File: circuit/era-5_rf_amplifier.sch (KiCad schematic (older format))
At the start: 9 parts, among them J1 CONN_01X04, J2 CONN_01X04, U1 ERA-5+

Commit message: rearranged schematics
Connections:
- net RFin: now reaches C1.2, J1.2 (P2), J1.3 (P3)
- net RFout: now reaches C2.1, J2.3 (P3)
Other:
- moved on the sheet: C1, C2, C3, L1, R1, R2
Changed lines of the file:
@@
 L C C1
 U 1 1 5931B134
-P 2550 2800
-F 0 "C1" H 2575 2900 50  0000 L CNN
-F 1 "0.1µF" H 2575 2700 50  0000 L CNN
-F 2 "" H 2588 2650 50  0001 C CNN
-F 3 "" H 2550 2800 50  0001 C CNN
-	1    2550 2800
+P 2850 2800
+F 0 "C1" H 2875 2900 50  0000 L CNN
+F 1 "0.1µF" H 2875 2700 50  0000 L CNN
+F 2 "" H 2888 2650 50  0001 C CNN
+F 3 "" H 2850 2800 50  0001 C CNN
+	1    2850 2800
 	0    1    1    0
 $EndComp
@@
 L C C2
 U 1 1 5931B1E4
-P 5150 2800
-F 0 "C2" H 5175 2900 50  0000 L CNN
-F 1 "0.1µF" H 5175 2700 50  0000 L CNN
-F 2 "" H 5188 2650 50  0001 C CNN
-F 3 "" H 5150 2800 50  0001 C CNN
-	1    5150 2800
+P 4800 2800
+F 0 "C2" H 4825 2900 50  0000 L CNN
+F 1 "0.1µF" H 4825 2700 50  0000 L CNN
+F 2 "" H 4838 2650 50  0001 C CNN
+F 3 "" H 4800 2800 50  0001 C CNN
+	1    4800 2800
 	0    1    1    0
 $EndComp
@@
 L L L1
 U 1 1 5931B2E5
-P 4850 2500
-F 0 "L1" V 4800 2500 50  0000 C CNN
-F 1 "1.59µH" V 4925 2500 50  0000 C CNN
-F 2 "" H 4850 2500 50  0001 C CNN
-F 3 "" H 4850 2500 50  0001 C CNN
-	1    4850 2500
+P 4500 2500
+F 0 "L1" V 4450 2500 50  0000 C CNN
+F 1 "1.59µH" V 4575 2500 50  0000 C CNN
+F 2 "" H 4500 2500 50  0001 C CNN
+F 3 "" H 4500 2500 50  0001 C CNN
+	1    4500 2500
 	1    0    0    -1
 $EndComp
@@
 L R R2
 U 1 1 5931B3DD
-P 5200 2050
-F 0 "R2" V 5280 2050 50  0000 C CNN
-F 1 "100R" V 5200 2050 50  0000 C CNN
-F 2 "" V 5130 2050 50  0001 C CNN
-F 3 "" H 5200 2050 50  0001 C CNN
-	1    5200 2050
+P 5200 1700
+F 0 "R2" V 5280 1700 50  0000 C CNN
+F 1 "100R" V 5200 1700 50  0000 C CNN
+F 2 "" V 5130 1700 50  0001 C CNN
+F 3 "" H 5200 1700 50  0001 C CNN
+	1    5200 1700
 	0    1    1    0
 $EndComp
@@
 L R R1
 U 1 1 5931B444
-P 5200 1850
-F 0 "R1" V 5280 1850 50  0000 C CNN
-F 1 "100R" V 5200 1850 50  0000 C CNN
-F 2 "" V 5130 1850 50  0001 C CNN
-F 3 "" H 5200 1850 50  0001 C CNN
-	1    5200 1850
+P 5200 1500
+F 0 "R1" V 5280 1500 50  0000 C CNN
+F 1 "100R" V 5200 1500 50  0000 C CNN
+F 2 "" V 5130 1500 50  0001 C CNN
+F 3 "" H 5200 1500 50  0001 C CNN
+	1    5200 1500
 	0    1    1    0
 $EndComp
@@
 L C C3
 U 1 1 5931B556
+P 5800 1850
+F 0 "C3" H 5825 1950 50  0000 L CNN
+F 1 "0.1µF" H 5825 1750 50  0000 L CNN
+F 2 "" H 5838 1700 50  0001 C CNN
+F 3 "" H 5800 1850 50  0001 C CNN
+	1    5800 1850
+	1    0    0    -1
+$EndComp
+$Comp
+L GND #PWR01
+U 1 1 5931B719
 P 5800 2200
-F 0 "C3" H 5825 2300 50  0000 L CNN
-F 1 "0.1µF" H 5825 2100 50  0000 L CNN
-F 2 "" H 5838 2050 50  0001 C CNN
+F 0 "#PWR01" H 5800 1950 50  0001 C CNN
+F 1 "GND" H 5800 2050 50  0000 C CNN
+F 2 "" H 5800 2200 50  0001 C CNN
 F 3 "" H 5800 2200 50  0001 C CNN
 	1    5800 2200
@@
 $EndComp
 $Comp
-L GND #PWR01
-U 1 1 5931B719
-P 5800 2550
-F 0 "#PWR01" H 5800 2300 50  0001 C CNN
-F 1 "GND" H 5800 2400 50  0000 C CNN
-F 2 "" H 5800 2550 50  0001 C CNN
-F 3 "" H 5800 2550 50  0001 C CNN
-	1    5800 2550
-	1    0    0    -1
-$EndComp
-$Comp
 L VCC #PWR02
 U 1 1 5931B73F
-P 5800 1550
-F 0 "#PWR02" H 5800 1400 50  0001 C CNN
-F 1 "VCC" H 5800 1700 50  0000 C CNN
-F 2 "" H 5800 1550 50  0001 C CNN
-F 3 "" H 5800 1550 50  0001 C CNN
-	1    5800 1550
-	1    0    0    -1
-$EndComp
-Wire Wire Line
-	5800 2350 5800 2550
-Wire Wire Line
-	5800 1550 5800 2050
-Wire Wire Line
-	5350 1850 5350 2050
-Wire Wire Line
-	5350 1950 5800 1950
-Connection ~ 5800 1950
-Connection ~ 5350 1950
-Wire Wire Line
-	5050 1850 5050 2050
-Wire Wire Line
-	4850 2350 4850 1950
-Wire Wire Line
-	4850 1950 5050 1950
-Connection ~ 5050 1950
-Wire Wire Line
-	4850 2650 4850 2800
-Wire Wire Line
-	4300 2800 5000 2800
+P 5800 1200
+F 0 "#PWR02" H 5800 1050 50  0001 C CNN
+F 1 "VCC" H 5800 1350 50  0000 C CNN
+F 2 "" H 5800 1200 50  0001 C CNN
+F 3 "" H 5800 1200 50  0001 C CNN
+	1    5800 1200
+	1    0    0    -1
+$EndComp
+Wire Wire Line
+	5800 2000 5800 2200
+Wire Wire Line
+	5800 1200 5800 1700
+Wire Wire Line
+	5350 1500 5350 1700
+Wire Wire Line
+	5350 1600 5800 1600
+Connection ~ 5800 1600
+Connection ~ 5350 1600
+Wire Wire Line
+	5050 1500 5050 1700
+Wire Wire Line
+	4500 1600 5050 1600
+Connection ~ 5050 1600
 $Comp
 L CONN_01X04 J1
@@
 	2050 2750 2050 2850
 Wire Wire Line
-	2050 2800 2400 2800
+	2050 2800 2700 2800
 Connection ~ 2050 2800
 $Comp
@@
 	2150 2950 2150 3150
 Wire Wire Line
-	5300 2800 5600 2800
+	4950 2800 5600 2800
 Wire Wire Line
 	5600 2800 5600 3350
@@
 Wire Wire Line
 	5200 3250 5200 3500
-Connection ~ 4850 2800
-Wire Wire Line
-	2700 2800 3100 2800
 $Comp
 L ERA-5+ U1
@@
 Wire Wire Line
 	1100 750  1100 900
+Text Label 5350 2800 0    60   ~ 0
+RFout
+Wire Wire Line
+	3000 2800 3100 2800
+Text Label 2450 2800 0    60   ~ 0
+RFin
+Wire Wire Line
+	4650 2800 4300 2800
+Wire Wire Line
+	4500 2650 4500 2800
+Connection ~ 4500 2800
+Wire Wire Line
+	4500 1600 4500 2350
 $EndSCHEMATC

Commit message: added some footprints
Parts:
- C1, C2, C3: footprint (none) -> Capacitors_SMD:C_1210_HandSoldering
- R1, R2: footprint (none) -> Resistors_SMD:R_1210_HandSoldering
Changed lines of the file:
@@
 LIBS:mc-amplifiers
 LIBS:rfcom
+LIBS:mc-chokes
 LIBS:era-5_rf_amplifier-cache
 EELAYER 25 0
@@
 F 0 "C1" H 2875 2900 50  0000 L CNN
 F 1 "0.1µF" H 2875 2700 50  0000 L CNN
-F 2 "" H 2888 2650 50  0001 C CNN
+F 2 "Capacitors_SMD:C_1210_HandSoldering" H 2888 2650 50  0001 C CNN
 F 3 "" H 2850 2800 50  0001 C CNN
 	1    2850 2800
@@
 F 0 "C2" H 4825 2900 50  0000 L CNN
 F 1 "0.1µF" H 4825 2700 50  0000 L CNN
-F 2 "" H 4838 2650 50  0001 C CNN
+F 2 "Capacitors_SMD:C_1210_HandSoldering" H 4838 2650 50  0001 C CNN
 F 3 "" H 4800 2800 50  0001 C CNN
 	1    4800 2800
@@
 F 0 "R2" V 5280 1700 50  0000 C CNN
 F 1 "100R" V 5200 1700 50  0000 C CNN
-F 2 "" V 5130 1700 50  0001 C CNN
+F 2 "Resistors_SMD:R_1210_HandSoldering" V 5130 1700 50  0001 C CNN
 F 3 "" H 5200 1700 50  0001 C CNN
 	1    5200 1700
@@
 F 0 "R1" V 5280 1500 50  0000 C CNN
 F 1 "100R" V 5200 1500 50  0000 C CNN
-F 2 "" V 5130 1500 50  0001 C CNN
+F 2 "Resistors_SMD:R_1210_HandSoldering" V 5130 1500 50  0001 C CNN
 F 3 "" H 5200 1500 50  0001 C CNN
 	1    5200 1500
@@
 F 0 "C3" H 5825 1950 50  0000 L CNN
 F 1 "0.1µF" H 5825 1750 50  0000 L CNN
-F 2 "" H 5838 1700 50  0001 C CNN
+F 2 "Capacitors_SMD:C_1210_HandSoldering" H 5838 1700 50  0001 C CNN
 F 3 "" H 5800 1850 50  0001 C CNN
 	1    5800 1850

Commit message: footprint for inductor
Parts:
- L1: footprint (none) -> Inductors_SMD:L_1812_HandSoldering
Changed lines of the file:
@@
 F 0 "L1" V 4450 2500 50  0000 C CNN
 F 1 "1.59µH" V 4575 2500 50  0000 C CNN
-F 2 "" H 4500 2500 50  0001 C CNN
+F 2 "Inductors_SMD:L_1812_HandSoldering" H 4500 2500 50  0001 C CNN
 F 3 "" H 4500 2500 50  0001 C CNN
 	1    4500 2500

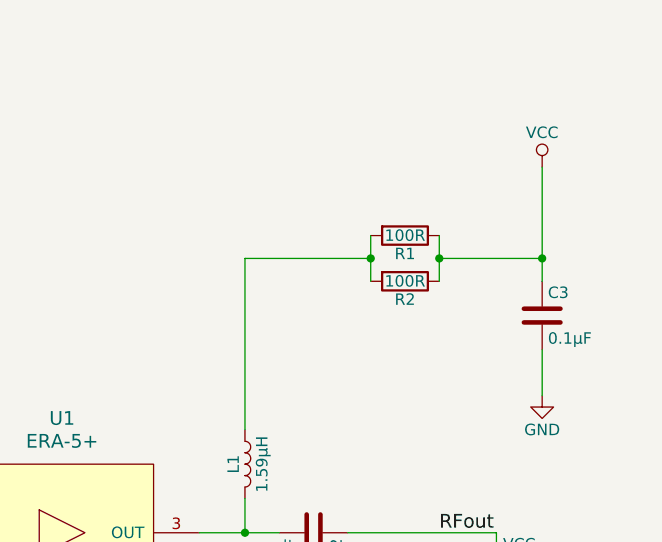
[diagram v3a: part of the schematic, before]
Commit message: Modified board schematic and layout
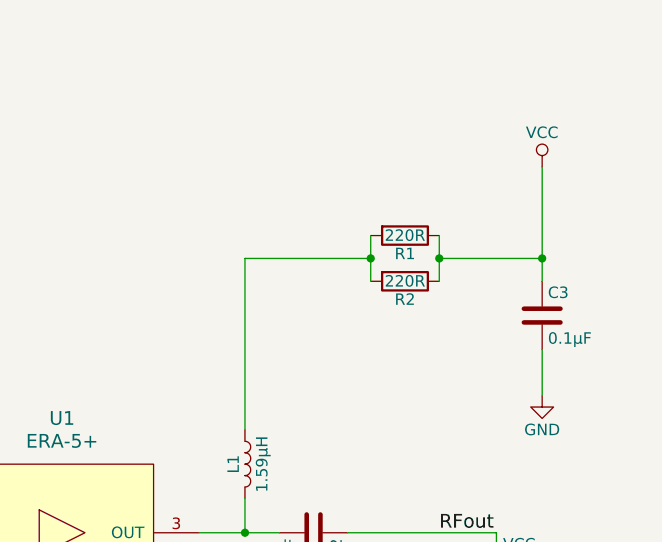
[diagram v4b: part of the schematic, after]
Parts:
- C1, C2, C3: footprint Capacitors_SMD:C_1210_HandSoldering -> Capacitors_SMD:C_1206_HandSoldering
- J1, J2: footprint Pin_Headers:Pin_Header_Straight_1x04_Pitch2.00mm -> Pin_Headers:Pin_Header_Straight_1x04_Pitch2.54mm
- R1, R2: value 100R -> 220R; footprint Resistors_SMD:R_1210_HandSoldering -> Resistors_SMD:R_1206_HandSoldering
- U1: footprint MiniCircuits:WW107 -> MiniCircuits:VV105
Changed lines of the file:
@@
 Sheet 1 1
 Title "ERA-5 amplifier"
-Date ""
+Date "2017-06-07"
 Rev ""
 Comp ""
@@
 F 0 "C1" H 2875 2900 50  0000 L CNN
 F 1 "0.1µF" H 2875 2700 50  0000 L CNN
-F 2 "Capacitors_SMD:C_1210_HandSoldering" H 2888 2650 50  0001 C CNN
+F 2 "Capacitors_SMD:C_1206_HandSoldering" H 2888 2650 50  0001 C CNN
 F 3 "" H 2850 2800 50  0001 C CNN
 	1    2850 2800
@@
 F 0 "C2" H 4825 2900 50  0000 L CNN
 F 1 "0.1µF" H 4825 2700 50  0000 L CNN
-F 2 "Capacitors_SMD:C_1210_HandSoldering" H 4838 2650 50  0001 C CNN
+F 2 "Capacitors_SMD:C_1206_HandSoldering" H 4838 2650 50  0001 C CNN
 F 3 "" H 4800 2800 50  0001 C CNN
 	1    4800 2800
@@
 P 5200 1700
 F 0 "R2" V 5280 1700 50  0000 C CNN
-F 1 "100R" V 5200 1700 50  0000 C CNN
-F 2 "Resistors_SMD:R_1210_HandSoldering" V 5130 1700 50  0001 C CNN
+F 1 "220R" V 5200 1700 50  0000 C CNN
+F 2 "Resistors_SMD:R_1206_HandSoldering" V 5130 1700 50  0001 C CNN
 F 3 "" H 5200 1700 50  0001 C CNN
 	1    5200 1700
@@
 P 5200 1500
 F 0 "R1" V 5280 1500 50  0000 C CNN
-F 1 "100R" V 5200 1500 50  0000 C CNN
-F 2 "Resistors_SMD:R_1210_HandSoldering" V 5130 1500 50  0001 C CNN
+F 1 "220R" V 5200 1500 50  0000 C CNN
+F 2 "Resistors_SMD:R_1206_HandSoldering" V 5130 1500 50  0001 C CNN
 F 3 "" H 5200 1500 50  0001 C CNN
 	1    5200 1500
@@
 F 0 "C3" H 5825 1950 50  0000 L CNN
 F 1 "0.1µF" H 5825 1750 50  0000 L CNN
-F 2 "Capacitors_SMD:C_1210_HandSoldering" H 5838 1700 50  0001 C CNN
+F 2 "Capacitors_SMD:C_1206_HandSoldering" H 5838 1700 50  0001 C CNN
 F 3 "" H 5800 1850 50  0001 C CNN
 	1    5800 1850
@@
 F 0 "J1" H 1850 3050 50  0000 C CNN
 F 1 "CONN_01X04" V 1950 2800 50  0000 C CNN
-F 2 "Pin_Headers:Pin_Header_Straight_1x04_Pitch2.00mm" H 1850 2800 50  0001 C CNN
+F 2 "Pin_Headers:Pin_Header_Straight_1x04_Pitch2.54mm" H 1850 2800 50  0001 C CNN
 F 3 "" H 1850 2800 50  0001 C CNN
 	1    1850 2800
@@
 F 0 "J2" H 5650 3800 50  0000 C CNN
 F 1 "CONN_01X04" V 5750 3550 50  0000 C CNN
-F 2 "Pin_Headers:Pin_Header_Straight_1x04_Pitch2.00mm" H 5650 3550 50  0001 C CNN
+F 2 "Pin_Headers:Pin_Header_Straight_1x04_Pitch2.54mm" H 5650 3550 50  0001 C CNN
 F 3 "" H 5650 3550 50  0001 C CNN
 	1    5650 3550
@@
 F 0 "U1" H 3700 3300 60  0000 C CNN
 F 1 "ERA-5+" H 3700 3200 60  0000 C CNN
-F 2 "MiniCircuits:WW107" H 3700 2800 60  0001 C CNN
+F 2 "MiniCircuits:VV105" H 3700 2800 60  0001 C CNN
 F 3 "" H 3700 2800 60  0000 C CNN
 	1    3700 2800
